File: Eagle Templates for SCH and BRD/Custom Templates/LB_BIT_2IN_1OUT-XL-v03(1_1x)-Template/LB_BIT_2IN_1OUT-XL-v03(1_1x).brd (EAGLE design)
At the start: 21.6 x 38 mm, 23 parts, among them U1 LV321SOT23-5, U2 LV321SOT23-5, U3 LV321SOT23-5

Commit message: added bitlab logo and made minor changes to board templates. Updated littlebits library.
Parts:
- added U$2: (no value), LITTLEBITS:BITLAB-LOGO
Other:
- board text added: "iX Name Here"
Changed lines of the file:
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@@
 <layer number="113" name="extra" color="10" fill="1" visible="yes" active="yes"/>
 <layer number="116" name="Patch_BOT" color="9" fill="4" visible="yes" active="yes"/>
+<layer number="118" name="Rect_Pads" color="7" fill="1" visible="no" active="yes"/>
 <layer number="121" name="_tsilk" color="7" fill="1" visible="yes" active="yes"/>
 <layer number="122" name="_bsilk" color="7" fill="1" visible="yes" active="yes"/>
@@
 <wire x1="24.12" y1="16.22" x2="24.12" y2="14.375" width="1" layer="46"/>
 <wire x1="23.62" y1="41.625" x2="23.405" y2="41.625" width="0" layer="20"/>
+<text x="19.8" y="30.8" size="1.3" layer="21" font="vector" rot="SR270" align="center">iX Name Here</text>
 </plain>
 <attributes>
@@
 <element name="U$3" library="LITTLEBITS" package="OSHWCREDIT" value="OSHWCREDIT" x="-95.12" y="-62.075"/>
 <element name="FRAME1" library="LITTLEBITS" package="FABDWG01-OHW" value="FRAME-LETTER" x="0" y="0"/>
+<element name="U$2" library="LITTLEBITS" package="BITLAB-LOGO" value="" x="18.3" y="34.9" rot="R270"/>
 </elements>
 <signals>

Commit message: Fixed input and output bitsnap connections
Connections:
- removed net SIG_IN: I32BSF1.SIG, I32BSM2.SIG1, I?R1.2, I?R2.2, I?R5.2, I?R6.2, I?TVS1.2, I?TVS3.2
- new net SIG1_IN: I32BSM1.SIG1, I?R5.2, I?R6.2, I?TVS3.2
- new net SIG2_IN: I32BSM2.SIG1, I?R1.2, I?R2.2, I?TVS1.2
- net GND: now also I32BSM1.GND1
- net SIG_OUT: now also I32BSF1.SIG
- net VCC: now also I32BSM1.VCC1
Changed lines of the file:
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@@
 <contactref element="I?C4" pad="1"/>
 <contactref element="U3" pad="5"/>
+<contactref element="I32BSM1" pad="VCC1"/>
+<wire x1="14.2249" y1="37.99" x2="15.75" y2="43.625" width="0" layer="19" extent="16-16"/>
 <wire x1="12.105" y1="37.985" x2="14.2249" y2="37.99" width="0" layer="19" extent="16-16"/>
 <wire x1="17.63" y1="28.33" x2="14.2249" y2="37.99" width="0" layer="19" extent="16-16"/>
@@
 <contactref element="I?TVS3" pad="1"/>
 <contactref element="I?R5" pad="1"/>
+<contactref element="I32BSM1" pad="GND1"/>
+<wire x1="11.98" y1="39.735" x2="14.685" y2="41.075" width="0" layer="19" extent="16-16"/>
+<wire x1="12.105" y1="36.285" x2="11.98" y2="39.735" width="0" layer="19" extent="16-16"/>
+<wire x1="10.67" y1="43.625" x2="11.98" y2="39.735" width="0" layer="19" extent="16-16"/>
+<wire x1="16.8251" y1="37.04" x2="14.685" y2="41.075" width="0" layer="19" extent="16-16"/>
+<wire x1="17.69" y1="32.505" x2="16.8251" y2="37.04" width="0" layer="19" extent="16-16"/>
+<wire x1="17.62" y1="30.4" x2="17.69" y2="32.505" width="0" layer="19" extent="16-16"/>
+<wire x1="19.305" y1="26.64" x2="17.62" y2="30.4" width="0" layer="19" extent="16-16"/>
+<wire x1="21.035" y1="25.92" x2="19.305" y2="26.64" width="0" layer="19" extent="16-16"/>
+<wire x1="15.865" y1="26.235" x2="19.305" y2="26.64" width="0" layer="19" extent="16-16"/>
+<wire x1="23.81" y1="28.96" x2="21.035" y2="25.92" width="0" layer="19" extent="16-16"/>
+<wire x1="16.67" y1="21.7799" x2="15.865" y2="26.235" width="0" layer="19" extent="16-16"/>
+<wire x1="15.04" y1="7.525" x2="16.67" y2="21.7799" width="0" layer="19" extent="16-16"/>
+<wire x1="13.35" y1="6" x2="15.04" y2="7.525" width="0" layer="19" extent="16-16"/>
+<wire x1="10.5249" y1="8.38" x2="13.35" y2="6" width="0" layer="19" extent="16-16"/>
+<wire x1="10.67" y1="3.44" x2="13.35" y2="6" width="0" layer="19" extent="16-16"/>
 </signal>
 <signal name="S$3">
@@
 <wire x1="15.72" y1="21.7799" x2="15.72" y2="24.3801" width="0" layer="19" extent="16-16"/>
 </signal>
-<signal name="SIG_IN">
-<contactref element="I?R2" pad="2"/>
-<contactref element="I?TVS1" pad="2"/>
-<contactref element="I?R1" pad="2"/>
-<contactref element="I32BSF1" pad="SIG"/>
-<contactref element="I32BSM2" pad="SIG1"/>
-<contactref element="I?R6" pad="2"/>
-<contactref element="I?TVS3" pad="2"/>
-<contactref element="I?R5" pad="2"/>
-<wire x1="15.11" y1="39.725" x2="15.685" y2="41.075" width="0" layer="19" extent="16-16"/>
-<wire x1="13.68" y1="39.735" x2="15.11" y2="39.725" width="0" layer="19" extent="16-16"/>
-<wire x1="19.305" y1="24.94" x2="15.11" y2="39.725" width="0" layer="19" extent="16-16"/>
-<wire x1="19.345" y1="23.32" x2="19.305" y2="24.94" width="0" layer="19" extent="16-16"/>
-<wire x1="21.035" y1="24.92" x2="19.305" y2="24.94" width="0" layer="19" extent="16-16"/>
-<wire x1="23.81" y1="26.42" x2="21.035" y2="24.92" width="0" layer="19" extent="16-16"/>
-<wire x1="13.21" y1="3.44" x2="19.345" y2="23.32" width="0" layer="19" extent="16-16"/>
-</signal>
 <signal name="N$4">
 <contactref element="U1" pad="1"/>
@@
 <contactref element="U2" pad="4"/>
 <contactref element="I?TVS2" pad="2"/>
+<contactref element="I32BSF1" pad="SIG"/>
 <wire x1="10.5249" y1="9.33" x2="13.1251" y2="9.33" width="0" layer="19" extent="16-16"/>
 <wire x1="12.35" y1="6" x2="13.1251" y2="9.33" width="0" layer="19" extent="16-16"/>
+<wire x1="13.21" y1="3.44" x2="12.35" y2="6" width="0" layer="19" extent="16-16"/>
 </signal>
 <signal name="N$3">
@@
 <wire x1="16.8251" y1="37.99" x2="16.81" y2="39.725" width="0" layer="19" extent="16-16"/>
 </signal>
+<signal name="SIG1_IN">
+<contactref element="I?R6" pad="2"/>
+<contactref element="I?TVS3" pad="2"/>
+<contactref element="I?R5" pad="2"/>
+<contactref element="I32BSM1" pad="SIG1"/>
+<wire x1="15.11" y1="39.725" x2="15.685" y2="41.075" width="0" layer="19" extent="16-16"/>
+<wire x1="13.68" y1="39.735" x2="15.11" y2="39.725" width="0" layer="19" extent="16-16"/>
+<wire x1="13.21" y1="43.625" x2="15.685" y2="41.075" width="0" layer="19" extent="16-16"/>
+</signal>
+<signal name="SIG2_IN">
+<contactref element="I?R2" pad="2"/>
+<contactref element="I?TVS1" pad="2"/>
+<contactref element="I?R1" pad="2"/>
+<contactref element="I32BSM2" pad="SIG1"/>
+<wire x1="21.035" y1="24.92" x2="23.81" y2="26.42" width="0" layer="19" extent="16-16"/>
+<wire x1="19.305" y1="24.94" x2="21.035" y2="24.92" width="0" layer="19" extent="16-16"/>
+<wire x1="19.345" y1="23.32" x2="19.305" y2="24.94" width="0" layer="19" extent="16-16"/>
+</signal>
 </signals>

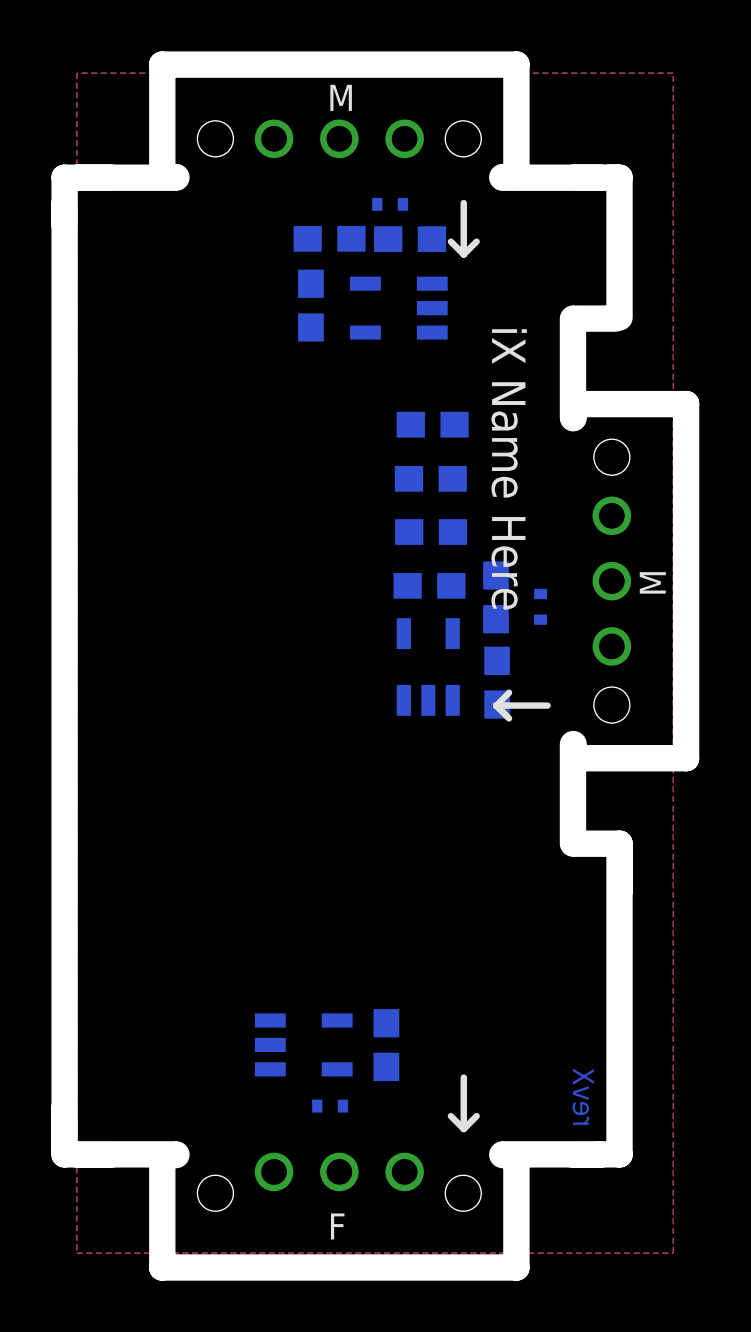
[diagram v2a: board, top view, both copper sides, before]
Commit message: Updated templates
- Added ferrite beads
- Moved text and annotations off of Nets layer
- Minor layout changes
- Removed I/O/W prefix from reference designators
- Removed output stage components from output bits
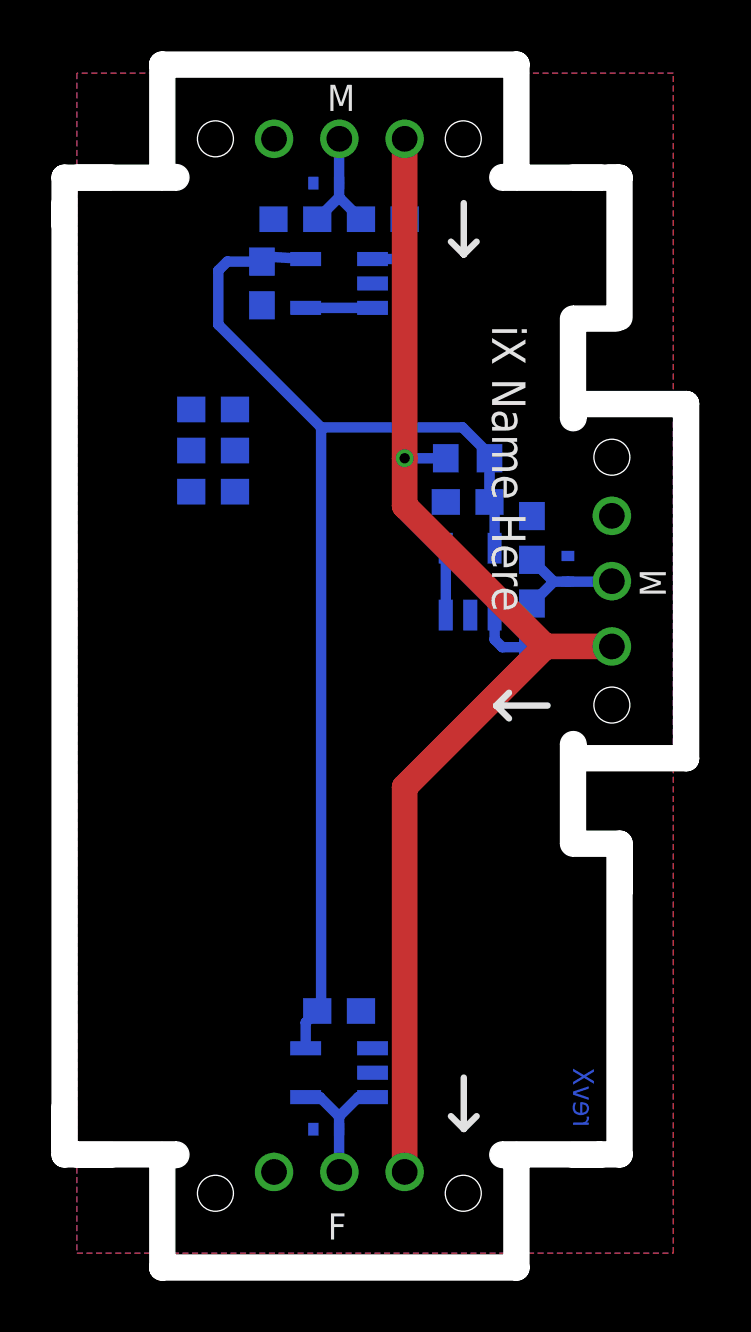
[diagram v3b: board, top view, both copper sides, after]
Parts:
- removed I?C1, I?C4: 0.1uF, LITTLEBITS:CAP-0603
- removed I?C2: 10uF, LITTLEBITS:CAP-0603
- removed I?C3: 1.0uF, LITTLEBITS:CAP-0603
- removed I?R1, I?R5: 1meg, LITTLEBITS:RES-0603
- removed I?R2, I?R6: 10K, LITTLEBITS:RES-0603
- removed I?R3, I?R4: 3K3, LITTLEBITS:RES-0603
- removed I?TVS1, I?TVS2, I?TVS3: ESD9B5.0ST5G, LITTLEBITS:SOD-923
- added C1, C3: 0.1uF, LITTLEBITS:CAP-0603
- added C2: 10uF, LITTLEBITS:CAP-0603
- added C4: 1.0uF, LITTLEBITS:CAP-0603
- added FB1: FERRITE-BEAD0603, LITTLEBITS:R0603
- added R1, R5: 1meg, LITTLEBITS:RES-0603
- added R2, R6: 10K, LITTLEBITS:RES-0603
- added R3, R4: 3K3, LITTLEBITS:RES-0603
- added TVS1, TVS2, TVS3: ESD9B5.0ST5G, LITTLEBITS:SOD-923
- moved U3 29.8 mm to (13.2, 7.30)
- moved U2 19.1 mm to (18.3, 26.4), turned to 0 degrees
- moved U1 15.3 mm to (13.2, 38.0), turned to 270 degrees
- renumbered I32BSF1 to BSF1, I32BSM1 to BSM1, I32BSM2 to BSM2
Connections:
- removed net N$3 (its old number): U2.1
- removed net N$5: I?R6.1, U3.1
- removed net SIG1_IN: BSM1.SIG1, I?R5.2, I?R6.2, I?TVS3.2
- removed net SIG2_IN: BSM2.SIG1, I?R1.2, I?R2.2, I?TVS1.2
- new net LB_VCC: BSF1.VCC, BSM1.VCC1, BSM2.VCC1, FB1.2
- new net N$12: U3.1
- new net N$2: R6.1, U2.1
- new net SIG_IN1: BSM1.SIG1, R1.2, R2.2, TVS1.2
- new net SIG_IN2: BSM2.SIG1, R5.2, R6.2, TVS2.2
- net GND: now also C1.2, C2.2, C3.2, C4.1, R1.1, R4.1, R5.1, TVS1.1, TVS2.1, TVS3.1; no longer I?C1.2, I?C2.2, I?C3.1, I?C4.2, I?R1.1, I?R4.1, I?R5.1, I?TVS1.1, I?TVS2.1, I?TVS3.1
- net N$1: now also U2.3, U2.4; no longer U3.3, U3.4
- net N$4: now also R2.1; no longer I?R2.1
- net SIG_OUT: now also TVS3.2, U3.3, U3.4; no longer I?TVS2.2, U2.3, U2.4
- net VCC: now also C1.1, C3.1, C4.2, FB1.1, R3.2; no longer BSF1.VCC, BSM1.VCC1, BSM2.VCC1, I?C1.1, I?C3.2, I?C4.1, I?R3.2
- net VREF: now also C2.1, R3.1, R4.2; no longer I?C2.1, I?R3.1, I?R4.2
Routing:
- net LB_VCC: track 0.00 -> 48.9 mm, vias 0 -> 1
- net VCC: track 0.00 -> 46.5 mm
- net SIG_OUT: track 0.00 -> 5.39 mm
- net SIG_IN1: track 0.00 -> 4.68 mm
- net SIG_IN2: track 0.00 -> 4.67 mm
- net N$3: track 0.00 -> 2.60 mm
- net N$1: track 0.00 -> 2.60 mm
- net N$4: track 0.00 -> 2.57 mm
- net N$2: track 0.00 -> 2.52 mm
